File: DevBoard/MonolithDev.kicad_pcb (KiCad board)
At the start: 4 copper layers, 196 x 115 mm, 362 parts, among them J101 Pack (welded 4S) - use instea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, J102 Cell 1 NTC 10k 103AT, J103 EV2400 SMBus, J104 Bench PACK_P, J105 Cell 2 NTC 10k 103AT, J106 Cell 3 NTC 10k 103AT, J107 Cell 4 NTC 10k 103AT, J301 SWD, J302 UART debug, J303 Spare GPIO, J401 TYPE-C 16PCB0.8 IP68, J402 I2CC logic analyzer, J501 TYPE-C 16PCB0.8 IP68, J502 I2CC logic analyzer, Q101 AGM404AP1, Q102 AGM404AP1, Q103 BSS138, Q401 IAUC45N04S6L063H, Q402 IAUC45N04S6L063H, Q501 IAUC45N04S6L063H, Q502 IAUC45N04S6L063H, SW101 WAKE, SW301 RESET, U101 BQ40Z50RSMR-R2, U201 INA190A5IDDFR, U202 INA190A1IDDFR, U203 TPS70950DBVR, U204 TPS62177DQCR, U301 STM32WB1MMC, U401 TPS25751DREFR, U402 M24512-DFMC6TG, U403 BQ25756RRVR, U404 TPS62933DRLR, U501 TPS25751DREFR, U502 M24512-DFMC6TG, U503 BQ25756RRVR, U504 TPS62933DRLR

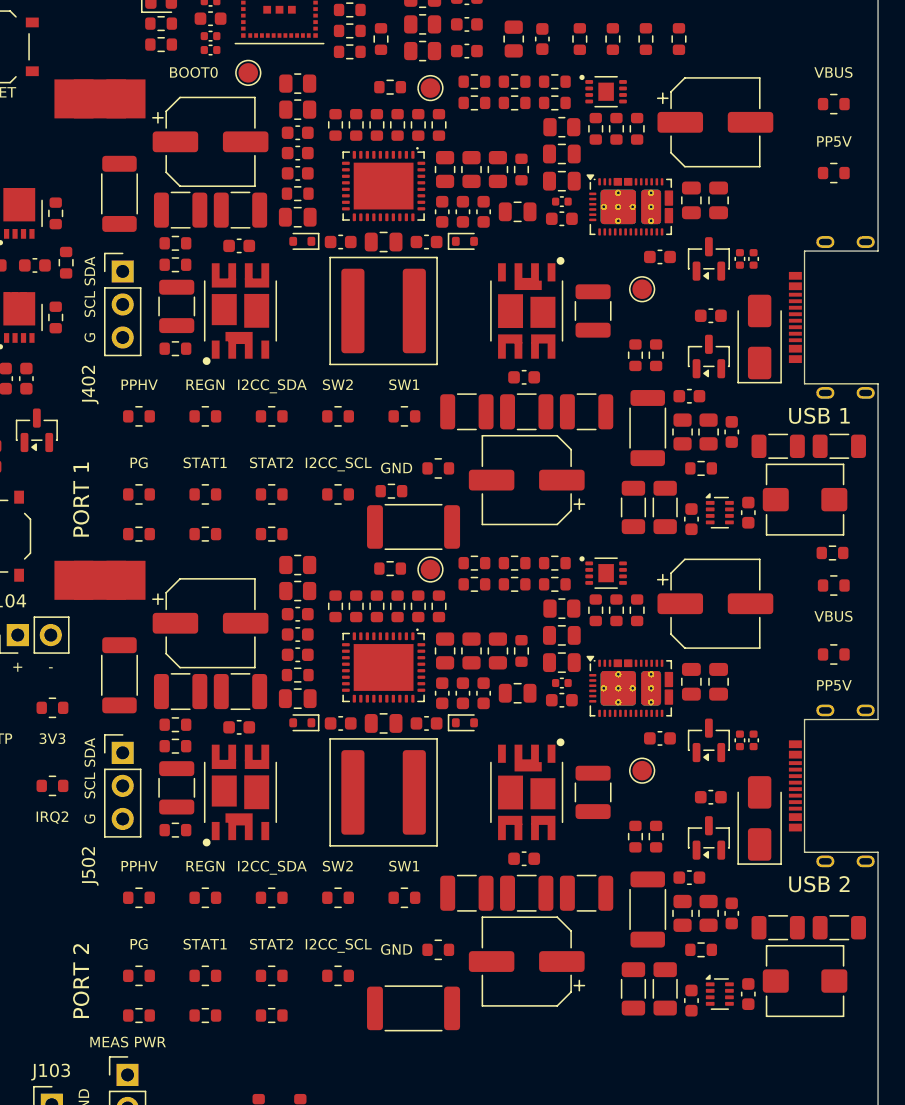
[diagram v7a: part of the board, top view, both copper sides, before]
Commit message: Dev board: start routing - planes, port power stages, gate drive, USB-C path, 5 V bucks
- Kelvin net class (0.2 mm / 0.15 mm) for the sense nets.
- tools/route_power.py (re-runnable, uuid sidecar): per port SW1/SW2 pours,
  input/output bank pours on F.Cu+B.Cu with GND islands stitched to In1,
  VBAT_SYS, gate drive on In2/B.Cu with F.Cu bootstrap loops, BQ25756 EP vias,
  VBUS and PPHV power path with RAC Kelvin taps, TPS62933 5 V buck and the
  PP5V feed to the TPS25751. In1 solid GND, In2 GND fill, M3 hole keep-outs.
- Placement: RBAT turned 180, SRP/SRN resistors beside it, gate-drive support
  parts regrouped ("fix" entries), C407/C507 0805 -> 0603 (CL10A106MA8NRNC,
  C96446) moved above U401 off the VBUS power pad.
- TPS25751 footprint: exposed-pad thermal vias solid to the planes.
- DRC 0 violations. README item 32.

Co-Authored-By: Claude Opus 5.5 <noreply@anthropic.com>
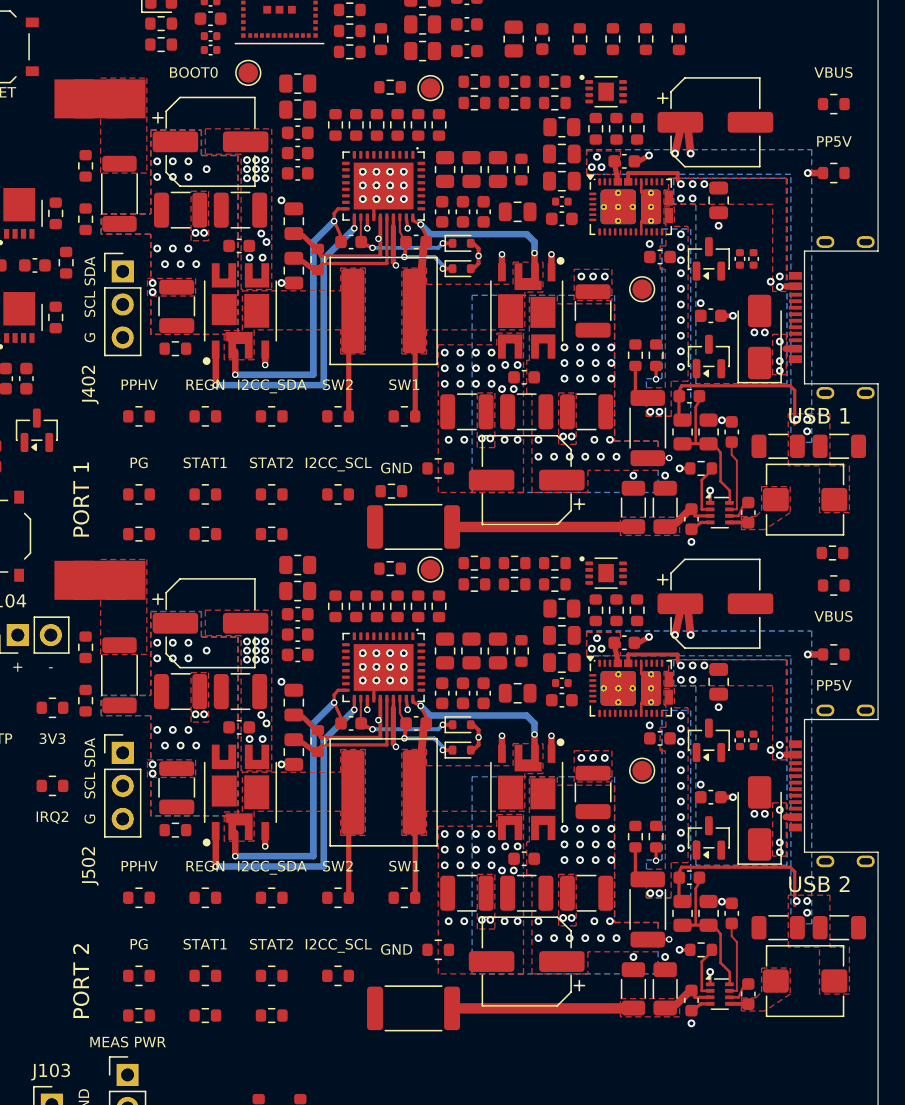
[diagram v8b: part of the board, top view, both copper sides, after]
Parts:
- C407, C507: footprint Capacitor_SMD:C_0805_2012Metric -> Capacitor_SMD:C_0603_1608Metric
- moved D405 12.3 mm to (214.0, 76.3), turned to 0 degrees
- moved D505 12.3 mm to (214.0, 113.3), turned to 0 degrees
- moved R429 10.3 mm to (185.1, 70.3), turned to -90 degrees
- moved R529 10.3 mm to (185.1, 107.3), turned to -90 degrees
- moved C410 7.24 mm to (201.1, 78.4), turned to -90 degrees
- moved C510 7.24 mm to (201.1, 115.4), turned to -90 degrees
- moved R428 7.14 mm to (185.1, 74.5), turned to 90 degrees
- moved R528 7.14 mm to (185.1, 111.5), turned to 90 degrees
- moved C407 5.96 mm to (226.5, 70.0), turned to 0 degrees
- moved C507 5.96 mm to (226.5, 107.0), turned to 0 degrees
- moved R420 5.30 mm to (202.9, 77.5), turned to 90 degrees
- moved R520 5.30 mm to (202.9, 114.5), turned to 90 degrees
- moved D404 2.11 mm to (214.0, 78.2)
- moved D504 2.11 mm to (214.0, 115.2)
- moved C412 0.80 mm to (210.5, 76.2), turned to 0 degrees
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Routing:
- net /USB Port 2/SW2: track 0.00 -> 27.8 mm, vias 0 -> 2
- net /USB Port 1/SW2: track 0.00 -> 27.8 mm, vias 0 -> 2
- net /USB Port 2/HG2: track 0.00 -> 24.8 mm, vias 0 -> 2
- net /USB Port 1/HG2: track 0.00 -> 24.8 mm, vias 0 -> 2
- net /USB Port 2/SW1: track 0.00 -> 19.7 mm, vias 0 -> 2
- net /USB Port 1/SW1: track 0.00 -> 19.7 mm, vias 0 -> 2
- net /USB Port 2/DRV_SUP: track 0.00 -> 19.5 mm, vias 0 -> 2
- net /USB Port 1/DRV_SUP: track 0.00 -> 19.5 mm, vias 0 -> 2
- net /USB Port 2/LG2: track 0.00 -> 19.2 mm, vias 0 -> 2
- net /USB Port 1/LG2: track 0.00 -> 19.2 mm, vias 0 -> 2
- net /USB Port 2/PP5V: track 0.00 -> 18.5 mm, vias 0 -> 9
- net /USB Port 1/PP5V: track 0.00 -> 18.5 mm, vias 0 -> 9
- net /USB Port 2/5V_IN: track 0.00 -> 14.9 mm
- net /USB Port 1/5V_IN: track 0.00 -> 14.9 mm
- net /USB Port 2/LG1: track 0.00 -> 14.6 mm, vias 0 -> 2
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- added copper zone on F.Cu, net /USB Port 1/5V_IN
- added copper zone on B.Cu, net /USB Port 1/AC_SNS_N
- added copper zone on F.Cu, net /USB Port 1/AC_SNS_N
- added copper zone on B.Cu, net /USB Port 1/BAT_SNS_P
- added copper zone on F.Cu, net /USB Port 1/BAT_SNS_P
- added copper zone on B.Cu, net /USB Port 1/PP5V
- added copper zone on F.Cu, net /USB Port 1/PP5V
- added copper zone on In2.Cu, net /USB Port 1/PP5V
- added copper zone on B.Cu, net /USB Port 1/PPHV
- added copper zone on F.Cu, net /USB Port 1/PPHV
- added copper zone on F.Cu, net /USB Port 1/SW1
- added copper zone on F.Cu, net /USB Port 1/SW2
- added copper zone on F.Cu, net /USB Port 1/SW_5V
- added copper zone on F.Cu, net /USB Port 1/VBAT_SYS
- added copper zone on B.Cu, net /USB Port 1/VBUS
- added copper zone on F.Cu, net /USB Port 1/VBUS
- added copper zone on F.Cu, net /USB Port 2/5V_IN
- added copper zone on B.Cu, net /USB Port 2/AC_SNS_N
- added copper zone on F.Cu, net /USB Port 2/AC_SNS_N
- added copper zone on B.Cu, net /USB Port 2/BAT_SNS_P
- added copper zone on F.Cu, net /USB Port 2/BAT_SNS_P
- added copper zone on B.Cu, net /USB Port 2/PP5V
- added copper zone on F.Cu, net /USB Port 2/PP5V
- added copper zone on In2.Cu, net /USB Port 2/PP5V
- added copper zone on B.Cu, net /USB Port 2/PPHV
- added copper zone on F.Cu, net /USB Port 2/PPHV
- added copper zone on F.Cu, net /USB Port 2/SW1
- added copper zone on F.Cu, net /USB Port 2/SW2
- added copper zone on F.Cu, net /USB Port 2/SW_5V
- added copper zone on F.Cu, net /USB Port 2/VBAT_SYS
- added copper zone on B.Cu, net /USB Port 2/VBUS
- added copper zone on F.Cu, net /USB Port 2/VBUS
- added copper zone on F.Cu, net GND
- added copper zone on In1.Cu, net GND
- added copper zone on In2.Cu, net GND
